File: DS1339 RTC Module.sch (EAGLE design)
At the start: 12 parts, among them U1 DS1339AU, Y1 ECS-.327-6-17X-TR

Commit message: Updated for Publishing
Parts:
- removed FD3: FIDUCIALUFIDUCIAL, SparkFun-Aesthetics:FIDUCIALUFIDUCIAL
- added LOGO1: OSHW-LOGOMINI, SparkFun-Aesthetics:OSHW-LOGOMINI
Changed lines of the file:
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@@
 <part name="FRAME1" library="SparkFun-Aesthetics" library_urn="urn:adsk.eagle:library:507" deviceset="FRAME-LETTER" device="" package3d_urn="urn:adsk.eagle:package:37121/1"/>
 <part name="FD2" library="SparkFun-Aesthetics" library_urn="urn:adsk.eagle:library:507" deviceset="FIDUCIAL" device="UFIDUCIAL" package3d_urn="urn:adsk.eagle:package:37111/1"/>
-<part name="FD3" library="SparkFun-Aesthetics" library_urn="urn:adsk.eagle:library:507" deviceset="FIDUCIAL" device="UFIDUCIAL" package3d_urn="urn:adsk.eagle:package:37111/1"/>
 <part name="J1" library="SparkFun-Connectors" library_urn="urn:adsk.eagle:library:513" deviceset="CONN_06" device="LOCK" package3d_urn="urn:adsk.eagle:package:38002/1"/>
 <part name="J2" library="SparkFun-Connectors" library_urn="urn:adsk.eagle:library:513" deviceset="CONN_02" device="" package3d_urn="urn:adsk.eagle:package:38039/1"/>
@@
 <part name="GND1" library="SparkFun-PowerSymbols" deviceset="GND" device=""/>
 <part name="Y1" library="DS1339 RTC Library" deviceset="ECS-.327-6-17X-TR" device=""/>
+<part name="LOGO1" library="SparkFun-Aesthetics" library_urn="urn:adsk.eagle:library:507" deviceset="OSHW-LOGO" device="MINI" package3d_urn="urn:adsk.eagle:package:37101/1"/>
 </parts>
 <sheets>
@@
 </instance>
 <instance part="FD2" gate="G$1" x="25.4" y="7.62" smashed="yes"/>
-<instance part="FD3" gate="G$1" x="33.02" y="7.62" smashed="yes"/>
 <instance part="J1" gate="G$1" x="104.14" y="55.88" smashed="yes">
 <attribute name="VALUE" x="99.06" y="45.974" size="1.778" layer="96" font="vector"/>
@@
 <attribute name="VALUE" x="121.655440625" y="73.64491875" size="1.78151875" layer="96"/>
 </instance>
+<instance part="LOGO1" gate="G$1" x="132.08" y="15.24" smashed="yes"/>
 </instances>
 <busses>

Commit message: Aesthetic Updates
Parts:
- renumbered BT1 to CR1225
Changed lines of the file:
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@@
 <part name="J1" library="SparkFun-Connectors" library_urn="urn:adsk.eagle:library:513" deviceset="CONN_06" device="LOCK" package3d_urn="urn:adsk.eagle:package:38002/1"/>
 <part name="J2" library="SparkFun-Connectors" library_urn="urn:adsk.eagle:library:513" deviceset="CONN_02" device="" package3d_urn="urn:adsk.eagle:package:38039/1"/>
-<part name="BT1" library="DS1339 RTC Library" deviceset="BATTERY" device="-12MM_SMD"/>
+<part name="CR1225" library="DS1339 RTC Library" deviceset="BATTERY" device="-12MM_SMD"/>
 <part name="R1" library="SparkFun-Resistors" deviceset="RESISTOR" device="0805" value=" "/>
 <part name="R2" library="SparkFun-Resistors" deviceset="RESISTOR" device="0805" value=" "/>
@@
 <attribute name="NAME" x="142.24" y="66.548" size="1.778" layer="95" font="vector"/>
 </instance>
-<instance part="BT1" gate="G$1" x="76.2" y="104.14" smashed="yes" rot="R270">
+<instance part="CR1225" gate="G$1" x="76.2" y="104.14" smashed="yes" rot="R270">
 <attribute name="NAME" x="80.518" y="104.14" size="1.778" layer="95" font="vector" rot="R270" align="bottom-center"/>
 <attribute name="VALUE" x="71.882" y="104.14" size="1.778" layer="96" font="vector" rot="R270" align="top-center"/>
@@
 <wire x1="152.4" y1="101.6" x2="162.56" y2="101.6" width="0.1524" layer="91"/>
 <wire x1="162.56" y1="101.6" x2="162.56" y2="91.44" width="0.1524" layer="91"/>
-<pinref part="BT1" gate="G$1" pin="-"/>
+<pinref part="CR1225" gate="G$1" pin="-"/>
 <wire x1="162.56" y1="91.44" x2="162.56" y2="88.9" width="0.1524" layer="91"/>
 <wire x1="76.2" y1="99.06" x2="76.2" y2="91.44" width="0.1524" layer="91"/>
@@
 <segment>
 <pinref part="U1" gate="A" pin="VBACKUP"/>
-<pinref part="BT1" gate="G$1" pin="+"/>
+<pinref part="CR1225" gate="G$1" pin="+"/>
 <wire x1="116.84" y1="114.3" x2="76.2" y2="114.3" width="0.1524" layer="91"/>
 <wire x1="76.2" y1="114.3" x2="76.2" y2="109.22" width="0.1524" layer="91"/>

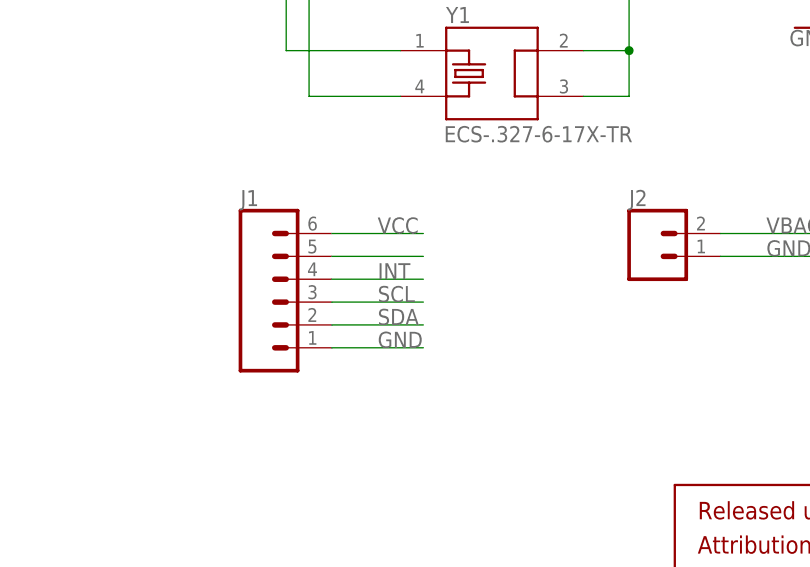
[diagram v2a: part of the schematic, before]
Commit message: Oops - Flipped VCC and GND on connector
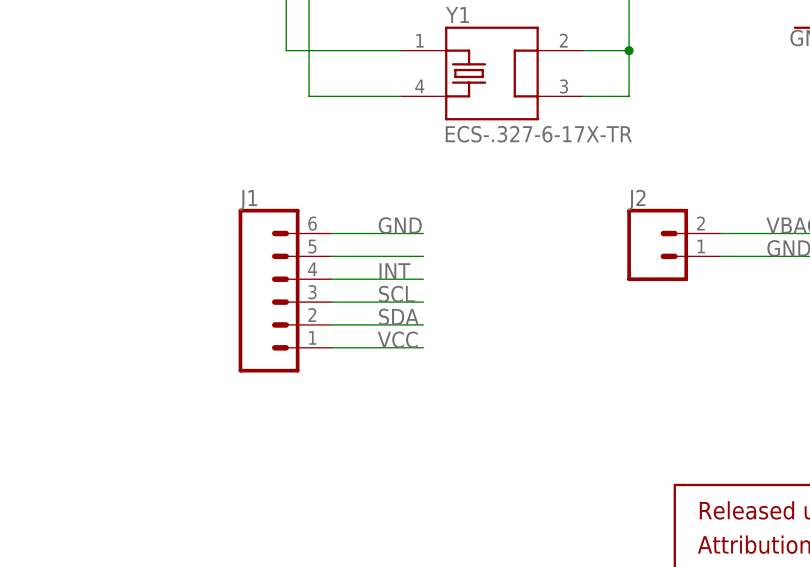
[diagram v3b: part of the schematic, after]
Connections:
- net GND: now also J1.6; no longer J1.1
- net VCC: now also J1.1; no longer J1.6
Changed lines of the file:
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@@
 </segment>
 <segment>
-<pinref part="J1" gate="G$1" pin="6"/>
-<wire x1="109.22" y1="63.5" x2="119.38" y2="63.5" width="0.1524" layer="91"/>
-<label x="114.3" y="63.5" size="1.778" layer="95"/>
+<pinref part="J1" gate="G$1" pin="1"/>
+<wire x1="109.22" y1="50.8" x2="119.38" y2="50.8" width="0.1524" layer="91"/>
+<label x="114.3" y="50.8" size="1.778" layer="95"/>
 </segment>
 </net>
@@
 </segment>
 <segment>
-<pinref part="J1" gate="G$1" pin="1"/>
-<wire x1="109.22" y1="50.8" x2="119.38" y2="50.8" width="0.1524" layer="91"/>
-<label x="114.3" y="50.8" size="1.778" layer="95"/>
-</segment>
-<segment>
 <pinref part="J2" gate="G$1" pin="1"/>
 <wire x1="152.4" y1="60.96" x2="162.56" y2="60.96" width="0.1524" layer="91"/>
 <label x="157.48" y="60.96" size="1.778" layer="95"/>
 </segment>
+<segment>
+<pinref part="J1" gate="G$1" pin="6"/>
+<wire x1="109.22" y1="63.5" x2="119.38" y2="63.5" width="0.1524" layer="91"/>
+<label x="114.3" y="63.5" size="1.778" layer="95"/>
+</segment>
 </net>

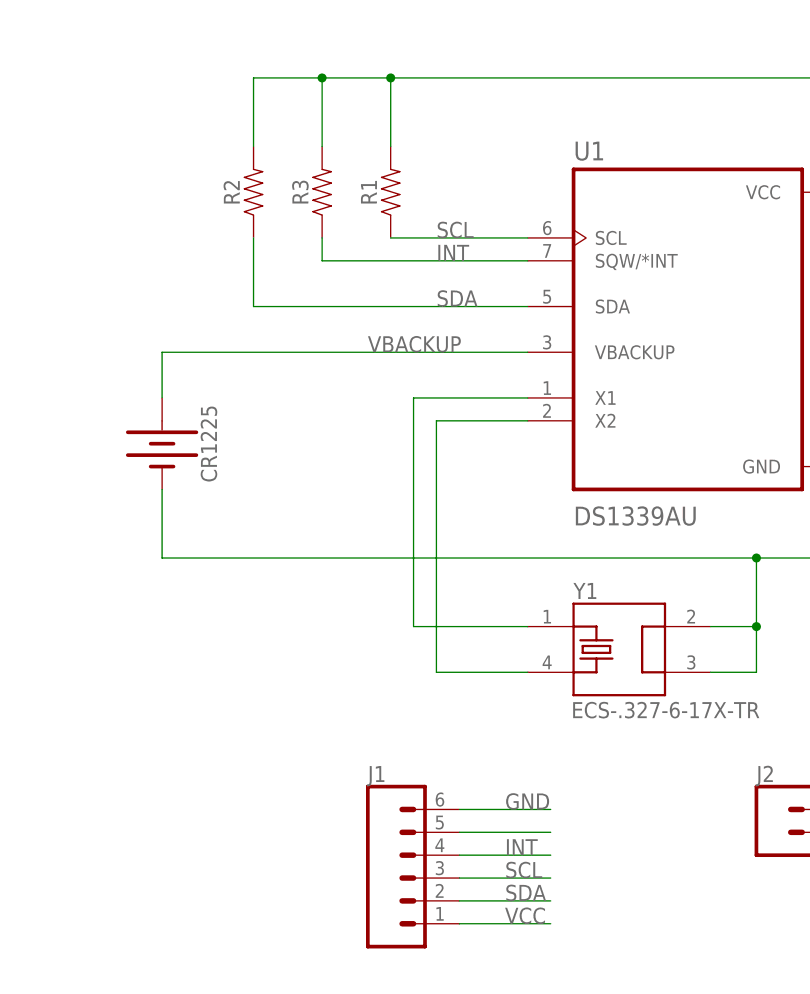
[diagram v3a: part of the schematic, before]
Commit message: Added BOM and values
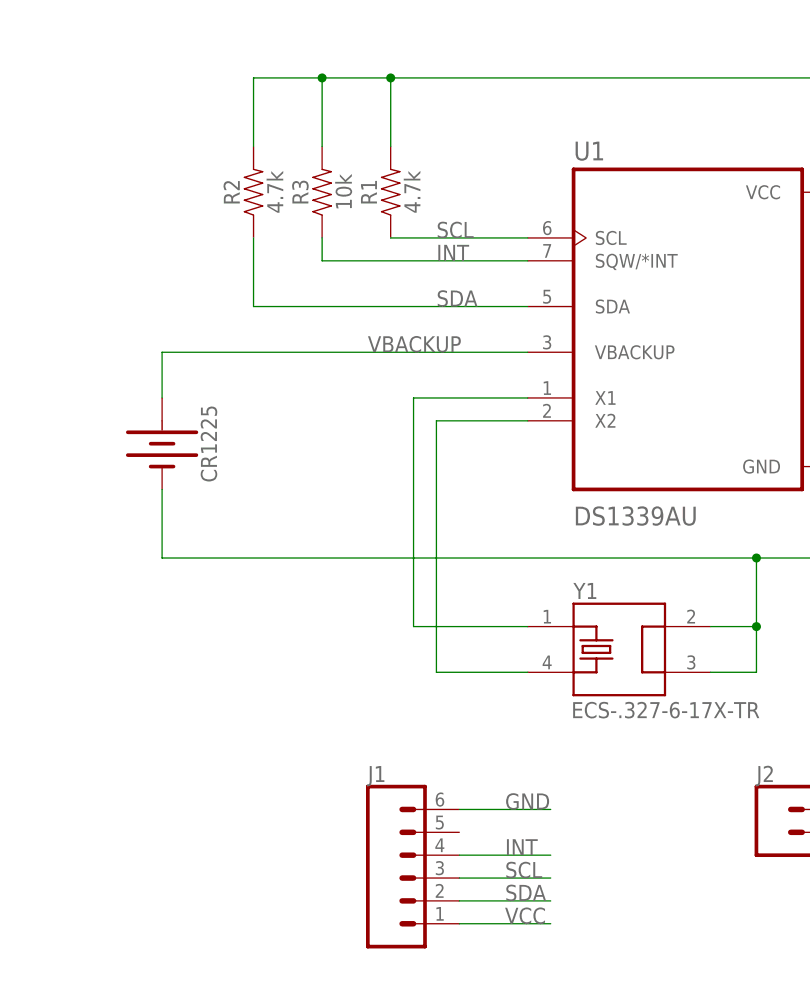
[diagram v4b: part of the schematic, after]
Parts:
- R1, R2: value (none) -> 4.7k
- R3: value (none) -> 10k
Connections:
- removed net N$8: J1.5
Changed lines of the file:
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@@
 <part name="J2" library="SparkFun-Connectors" library_urn="urn:adsk.eagle:library:513" deviceset="CONN_02" device="" package3d_urn="urn:adsk.eagle:package:38039/1"/>
 <part name="CR1225" library="DS1339 RTC Library" deviceset="BATTERY" device="-12MM_SMD"/>
-<part name="R1" library="SparkFun-Resistors" deviceset="RESISTOR" device="0805" value=" "/>
-<part name="R2" library="SparkFun-Resistors" deviceset="RESISTOR" device="0805" value=" "/>
-<part name="R3" library="SparkFun-Resistors" deviceset="RESISTOR" device="0805" value=" "/>
+<part name="R1" library="SparkFun-Resistors" deviceset="RESISTOR" device="0805" value="4.7k"/>
+<part name="R2" library="SparkFun-Resistors" deviceset="RESISTOR" device="0805" value="4.7k"/>
+<part name="R3" library="SparkFun-Resistors" deviceset="RESISTOR" device="0805" value="10k"/>
 <part name="SUPPLY1" library="SparkFun-PowerSymbols" library_urn="urn:adsk.eagle:library:530" deviceset="VCC" device=""/>
 <part name="GND1" library="SparkFun-PowerSymbols" deviceset="GND" device=""/>
@@
 </segment>
 </net>
-<net name="N$8" class="0">
-<segment>
-<pinref part="J1" gate="G$1" pin="5"/>
-<wire x1="109.22" y1="60.96" x2="119.38" y2="60.96" width="0.1524" layer="91"/>
-</segment>
-</net>
